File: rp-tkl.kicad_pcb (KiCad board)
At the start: 2 copper layers, 344.7 x 123.1 mm, 0 parts

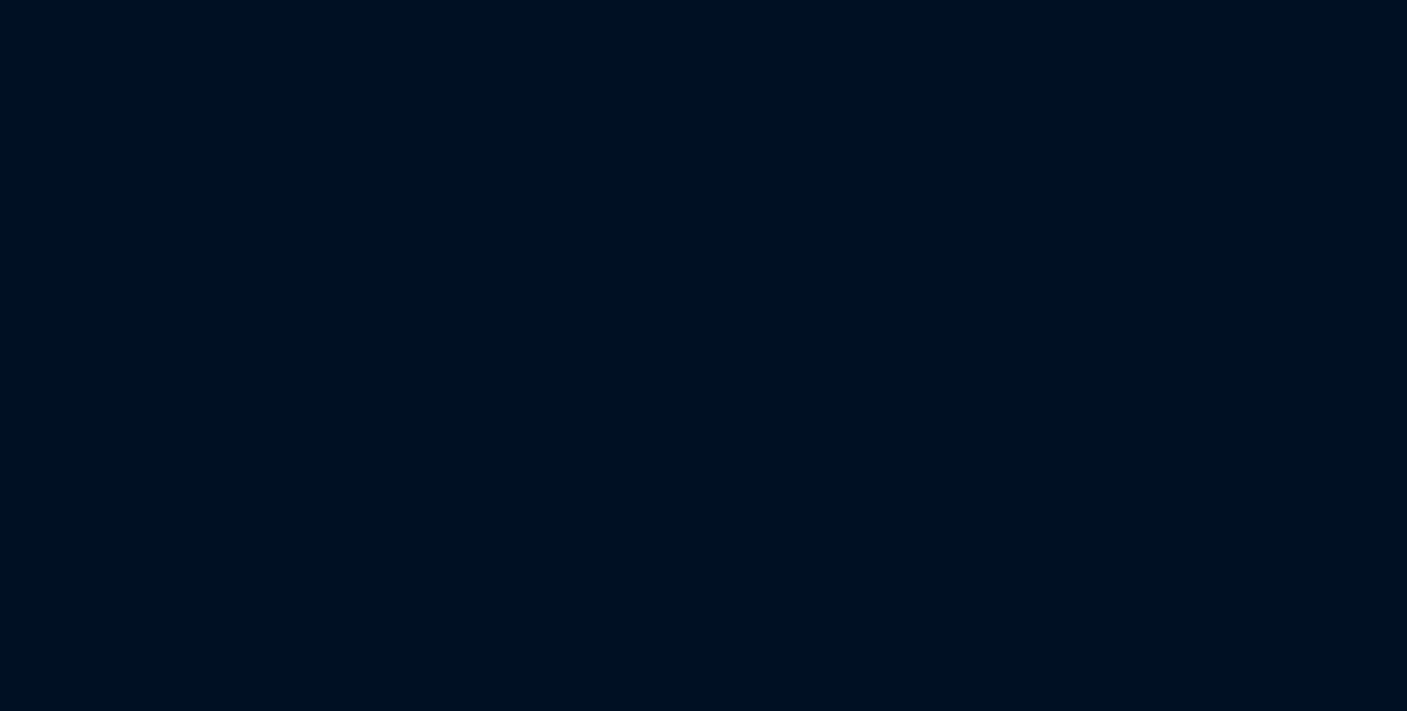
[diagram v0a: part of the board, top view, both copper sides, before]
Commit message: Added Footprint Libs, Annotated schematic, Imported footprints
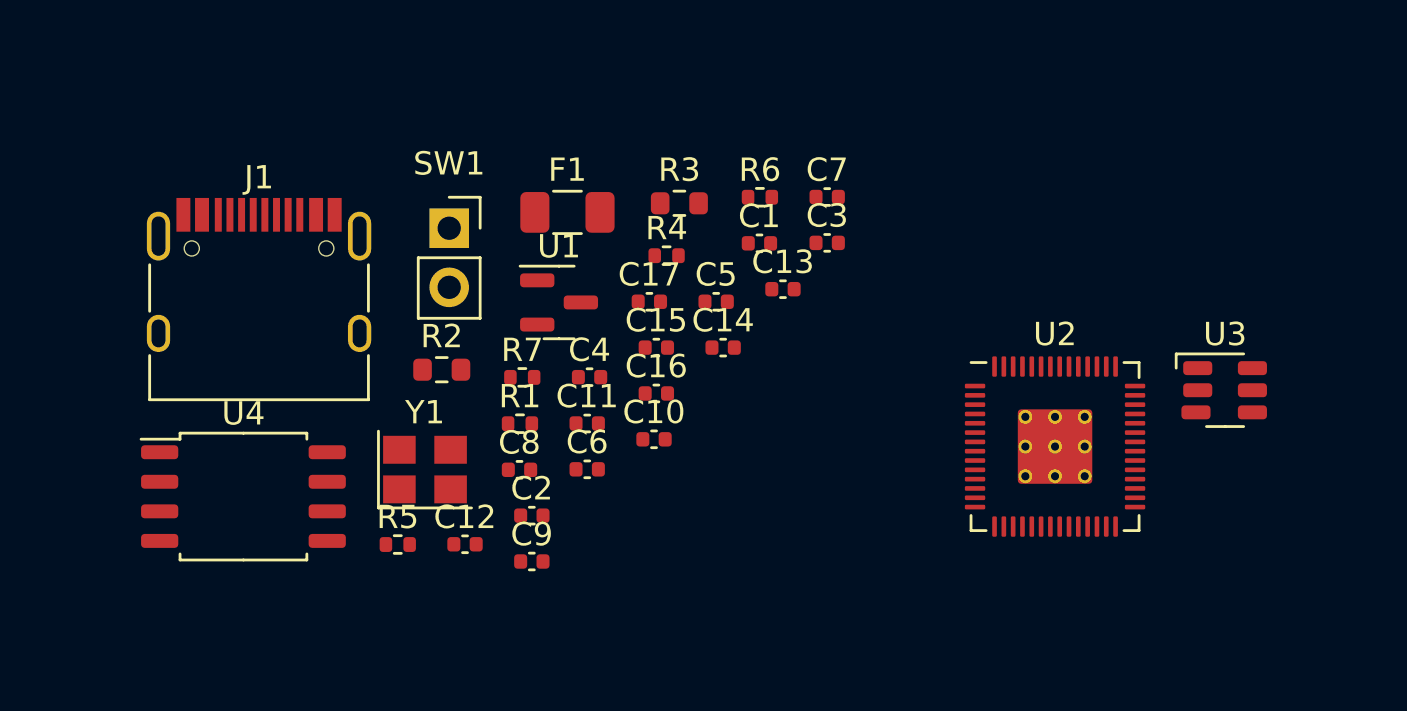
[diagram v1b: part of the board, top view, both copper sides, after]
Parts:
- added C1: 1uF, Capacitor_SMD:C_0402_1005Metric, F.Cu at (213.9, 104.2)
- added C10: 100nF, Capacitor_SMD:C_0402_1005Metric, F.Cu at (209.4, 112.6)
- added C11: 100nF, Capacitor_SMD:C_0402_1005Metric, F.Cu at (206.5, 111.9)
- added C12: 100nF, Capacitor_SMD:C_0402_1005Metric, F.Cu at (201.3, 117.1)
- added C13: 1uF, Capacitor_SMD:C_0402_1005Metric, F.Cu at (214.9, 106.2)
- added C14: 1uF, Capacitor_SMD:C_0402_1005Metric, F.Cu at (212.4, 108.7)
- added C15: 22pF, Capacitor_SMD:C_0402_1005Metric, F.Cu at (209.5, 108.7)
- added C16: 22pF, Capacitor_SMD:C_0402_1005Metric, F.Cu at (209.5, 110.6)
- added C17: 100nF, Capacitor_SMD:C_0402_1005Metric, F.Cu at (209.2, 106.7)
- added C2: 100nF, Capacitor_SMD:C_0402_1005Metric, F.Cu at (204.1, 115.9)
- added C3: 100nF, Capacitor_SMD:C_0402_1005Metric, F.Cu at (216.8, 104.2)
- added C4: 10uF, Capacitor_SMD:C_0402_1005Metric, F.Cu at (206.6, 109.9)
- added C5: 1uF, Capacitor_SMD:C_0402_1005Metric, F.Cu at (212.1, 106.7)
- added C6: 100nF, Capacitor_SMD:C_0402_1005Metric, F.Cu at (206.5, 113.9)
- added C7: 100nF, Capacitor_SMD:C_0402_1005Metric, F.Cu at (216.8, 102.2)
- added C8: 100nF, Capacitor_SMD:C_0402_1005Metric, F.Cu at (203.6, 113.9)
- added C9: 100nF, Capacitor_SMD:C_0402_1005Metric, F.Cu at (204.1, 117.9)
- added F1: 500mA, Fuse:Fuse_1206_3216Metric, F.Cu at (205.7, 102.9)
- added J1: USB_C_Receptacle_USB2.0, Connector_USB:USB_C_Receptacle_HRO_TYPE-C-31-M-12, F.Cu at (192.4, 107.0)
- added R1: 10k, Resistor_SMD:R_0402_1005Metric, F.Cu at (203.6, 111.9)
- added R2: 27R, Resistor_SMD:R_0603_1608Metric, F.Cu at (200.3, 109.6)
- added R3: 27R, Resistor_SMD:R_0603_1608Metric, F.Cu at (210.5, 102.5)
- added R4: 1k, Resistor_SMD:R_0402_1005Metric, F.Cu at (209.9, 104.7)
- added R5: 1k, Resistor_SMD:R_0402_1005Metric, F.Cu at (198.4, 117.1)
- added R6: 5.1k, Resistor_SMD:R_0402_1005Metric, F.Cu at (213.9, 102.2)
- added R7: 5.1k, Resistor_SMD:R_0402_1005Metric, F.Cu at (203.7, 110.0)
- added SW1: SW_Push, Connector_PinSocket_2.54mm:PinSocket_1x02_P2.54mm_Vertical, F.Cu at (200.6, 103.5)
- added U1: XC6206PxxxMR, Package_TO_SOT_SMD:SOT-23, F.Cu at (205.3, 106.7)
- added U2: RP2040, Sleep-lib:RP2040-QFN-56, F.Cu at (226.6, 112.9)
- added U3: SRV05-4, marbastlib-various:SOT-23-6-routable, F.Cu at (233.9, 110.5)
- added U4: W25Q128JVS, Package_SO:SOIC-8_5.23x5.23mm_P1.27mm, F.Cu at (191.8, 115.1)
- added Y1: 12MHz, Crystal:Crystal_SMD_3225-4Pin_3.2x2.5mm, F.Cu at (199.6, 113.9)

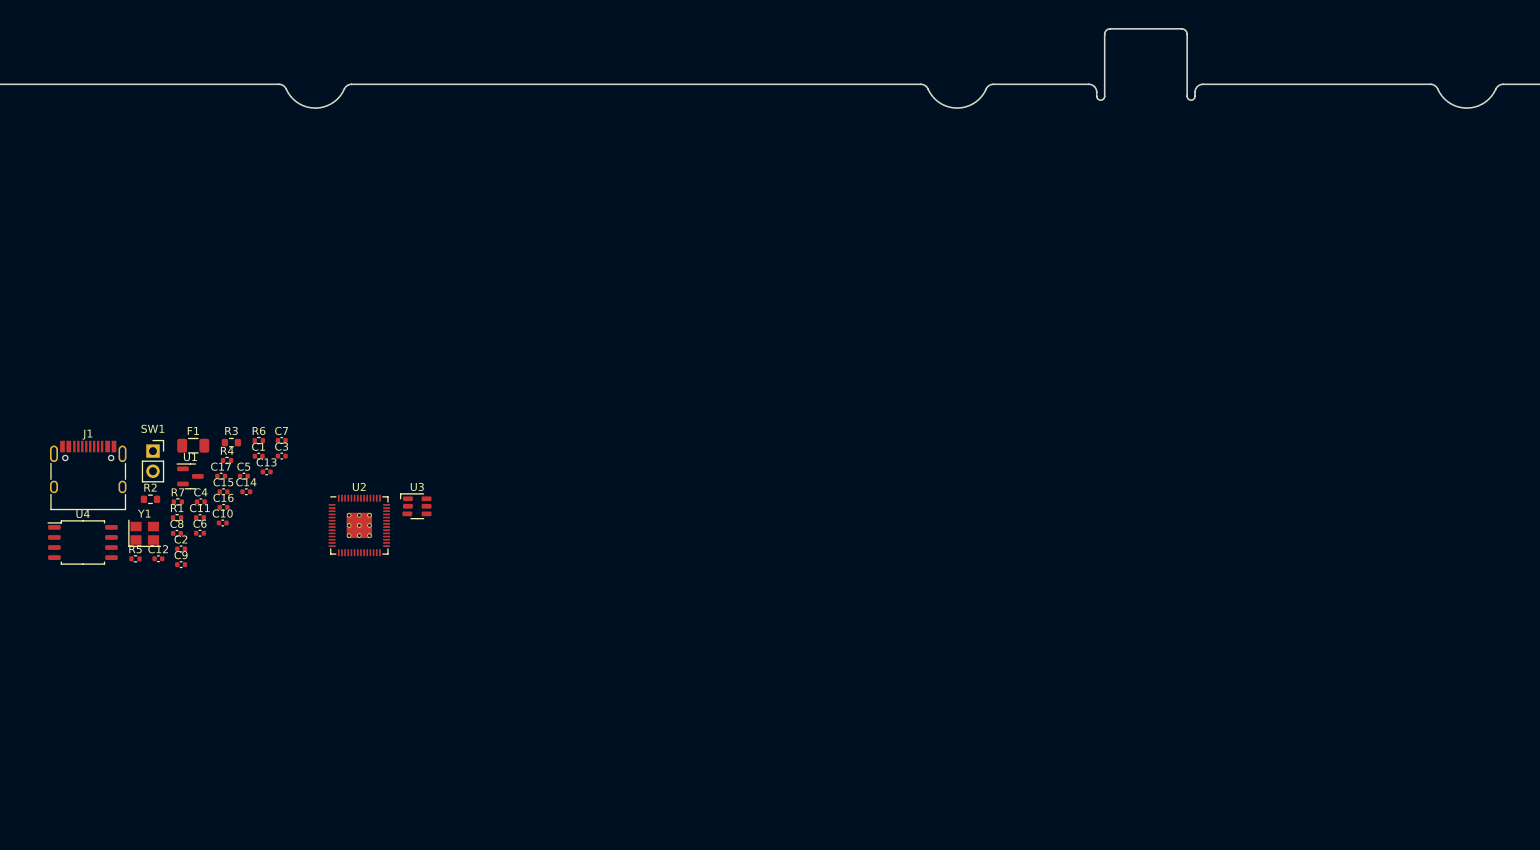
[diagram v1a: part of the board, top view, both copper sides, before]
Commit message: [Excluding Switches] Moved components to rough positions on pcb
Also added 5 pin programming header
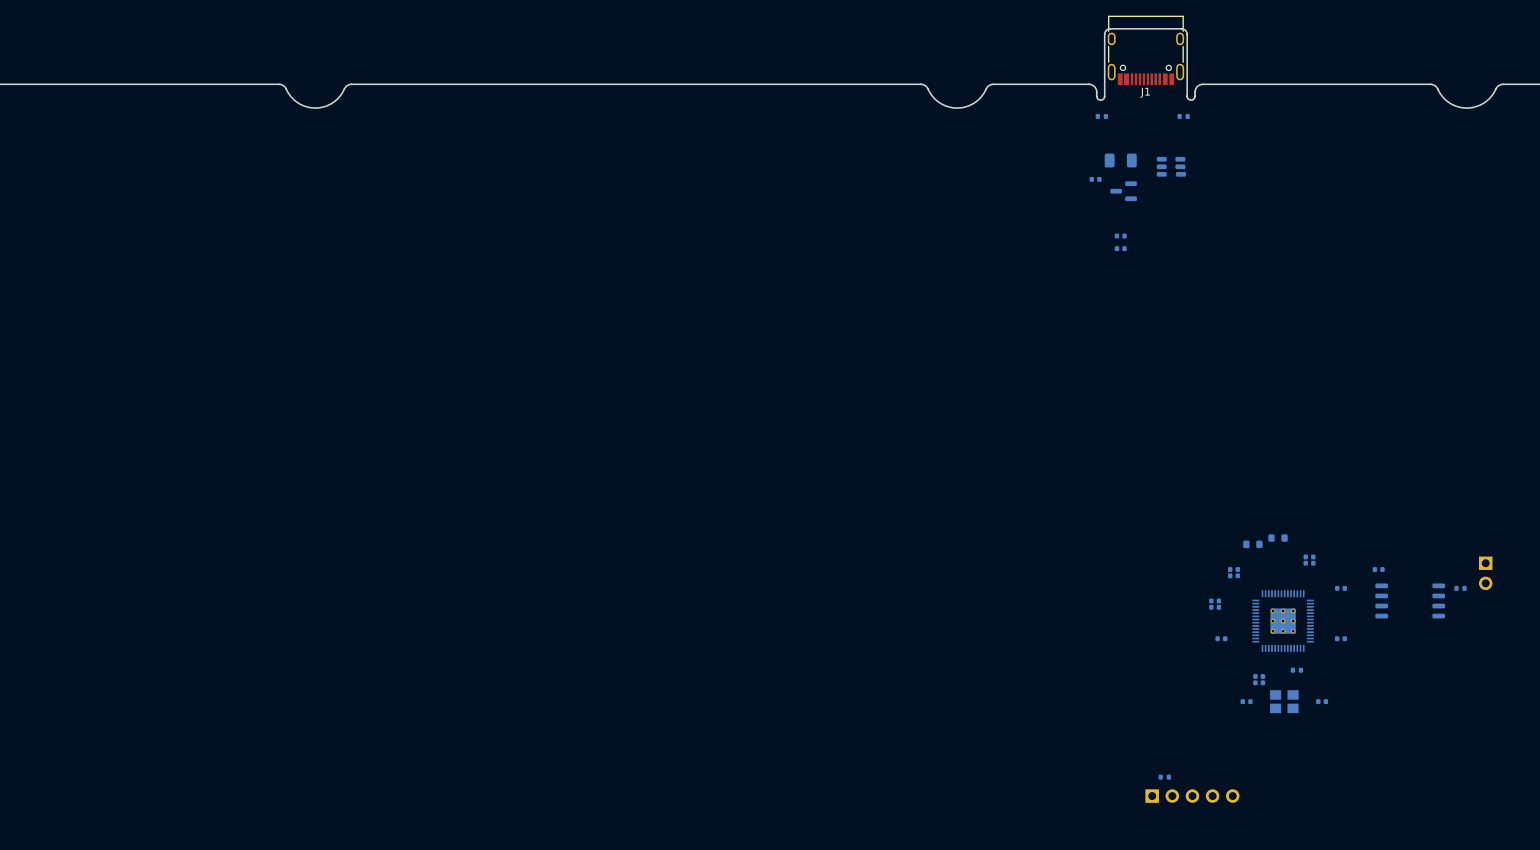
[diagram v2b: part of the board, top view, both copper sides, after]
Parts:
- added J2: SWD, Connector_PinSocket_2.54mm:PinSocket_1x05_P2.54mm_Vertical, B.Cu at (326.6, 147.1)
- C1, C10, C11, C12, C13, C14, C15, C16, C17, C2, C3, C4, C5, C6, C7, C8, C9, F1, R1, R2, R3, R4, R5, R6, R7, SW1, U1, U2, U3, U4, Y1: moved to B.Cu
- moved SW1 168.7 mm to (368.7, 117.7), turned to 180 degrees
- moved U4 167.6 mm to (359.2, 122.5), turned to 180 degrees
- moved R5 167.2 mm to (365.5, 120.9), turned to 180 degrees
- moved C12 149.2 mm to (350.5, 120.9), turned to 180 degrees
- moved C8 147.4 mm to (350.5, 127.2), turned to 180 degrees
- moved C17 146.5 mm to (355.2, 118.5), turned to 180 degrees
- moved Y1 145.3 mm to (343.3, 135.2), turned to 180 degrees
- moved J1 144.1 mm to (325.8, 52.6), turned to 180 degrees
- moved C16 140.7 mm to (348.1, 135.2), turned to 180 degrees
- moved R2 139.2 mm to (339.3, 115.3), turned to 180 degrees
- moved R4 137.5 mm to (344.9, 131.2), turned to 180 degrees
- moved C2 136.9 mm to (340.1, 132.0), turned to 180 degrees
- moved C9 136.8 mm to (340.1, 132.8), turned to 180 degrees
- moved R3 132.6 mm to (342.5, 114.5), turned to 180 degrees
- moved C15 131.7 mm to (338.5, 135.2), turned to 180 degrees
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
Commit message: [Preliminary] Added Switch matrix and imported footprints
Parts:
- added D1: D, Diode_SMD:D_0402_1005Metric, B.Cu at (686.1, 243.1)
- added D10: D, Diode_SMD:D_0402_1005Metric, B.Cu at (466.5, 79.8)
- added D11: D, Diode_SMD:D_0402_1005Metric, B.Cu at (723.8, 241.1)
- added D12: D, Diode_SMD:D_0402_1005Metric, B.Cu at (705.0, 241.1)
- added D13: D, Diode_SMD:D_0402_1005Metric, B.Cu at (506.9, 120.1)
- added D14: D, Diode_SMD:D_0402_1005Metric, B.Cu at (726.9, 241.1)
- added D15: D, Diode_SMD:D_0402_1005Metric, B.Cu at (446.4, 59.6)
- added D16: D, Diode_SMD:D_0402_1005Metric, B.Cu at (698.7, 241.1)
- added D17: D, Diode_SMD:D_0402_1005Metric, B.Cu at (629.6, 243.1)
- added D18: D, Diode_SMD:D_0402_1005Metric, B.Cu at (739.5, 241.1)
- added D19: D, Diode_SMD:D_0402_1005Metric, B.Cu at (645.3, 241.1)
- added D2: D, Diode_SMD:D_0402_1005Metric, B.Cu at (673.6, 241.1)
- added D20: D, Diode_SMD:D_0402_1005Metric, B.Cu at (446.4, 61.6)
- added D21: D, Diode_SMD:D_0402_1005Metric, B.Cu at (506.9, 122.1)
- added D22: D, Diode_SMD:D_0402_1005Metric, B.Cu at (486.7, 101.9)
- added D23: D, Diode_SMD:D_0402_1005Metric, B.Cu at (654.7, 241.1)
- added D24: D, Diode_SMD:D_0402_1005Metric, B.Cu at (745.8, 241.1)
- added D25: D, Diode_SMD:D_0402_1005Metric, B.Cu at (483.6, 99.9)
- added D26: D, Diode_SMD:D_0402_1005Metric, B.Cu at (679.8, 241.1)
- added D27: D, Diode_SMD:D_0402_1005Metric, B.Cu at (717.5, 241.1)
- added D28: D, Diode_SMD:D_0402_1005Metric, B.Cu at (733.2, 243.1)
- added D29: D, Diode_SMD:D_0402_1005Metric, B.Cu at (664.1, 241.1)
- added D3: D, Diode_SMD:D_0402_1005Metric, B.Cu at (711.2, 243.1)
- added D30: D, Diode_SMD:D_0402_1005Metric, B.Cu at (651.6, 241.1)
- added D31: D, Diode_SMD:D_0402_1005Metric, B.Cu at (692.4, 241.1)
- added D32: D, Diode_SMD:D_0402_1005Metric, B.Cu at (676.7, 243.1)
- added D33: D, Diode_SMD:D_0402_1005Metric, B.Cu at (670.4, 241.1)
- added D34: D, Diode_SMD:D_0402_1005Metric, B.Cu at (708.1, 241.1)
- added D35: D, Diode_SMD:D_0402_1005Metric, B.Cu at (654.7, 243.1)
- added D36: D, Diode_SMD:D_0402_1005Metric, B.Cu at (632.7, 243.1)
- added D37: D, Diode_SMD:D_0402_1005Metric, B.Cu at (720.7, 243.1)
- added D38: D, Diode_SMD:D_0402_1005Metric, B.Cu at (683.0, 243.1)
- added D39: D, Diode_SMD:D_0402_1005Metric, B.Cu at (639.0, 241.1)
- added D4: D, Diode_SMD:D_0402_1005Metric, B.Cu at (657.9, 243.1)
- added D40: D, Diode_SMD:D_0402_1005Metric, B.Cu at (629.6, 241.1)
- added D41: D, Diode_SMD:D_0402_1005Metric, B.Cu at (664.1, 243.1)
- added D42: D, Diode_SMD:D_0402_1005Metric, B.Cu at (692.4, 243.1)
- added D43: D, Diode_SMD:D_0402_1005Metric, B.Cu at (651.6, 243.1)
- added D44: D, Diode_SMD:D_0402_1005Metric, B.Cu at (648.4, 241.1)
- added D45: D, Diode_SMD:D_0402_1005Metric, B.Cu at (730.1, 243.1)
- added D46: D, Diode_SMD:D_0402_1005Metric, B.Cu at (748.9, 241.1)
- added D47: D, Diode_SMD:D_0402_1005Metric, B.Cu at (701.8, 241.1)
- added D48: D, Diode_SMD:D_0402_1005Metric, B.Cu at (642.2, 241.1)
- added D49: D, Diode_SMD:D_0402_1005Metric, B.Cu at (679.8, 243.1)
- added D5: D, Diode_SMD:D_0402_1005Metric, B.Cu at (714.4, 243.1)
- added D50: D, Diode_SMD:D_0402_1005Metric, B.Cu at (720.7, 241.1)
- added D51: D, Diode_SMD:D_0402_1005Metric, B.Cu at (639.0, 243.1)
- added D52: D, Diode_SMD:D_0402_1005Metric, B.Cu at (657.9, 241.1)
- added D53: D, Diode_SMD:D_0402_1005Metric, B.Cu at (683.0, 241.1)
- added D54: D, Diode_SMD:D_0402_1005Metric, B.Cu at (689.3, 243.1)
- added D55: D, Diode_SMD:D_0402_1005Metric, B.Cu at (661.0, 241.1)
- added D56: D, Diode_SMD:D_0402_1005Metric, B.Cu at (635.9, 241.1)
- added D57: D, Diode_SMD:D_0402_1005Metric, B.Cu at (466.5, 81.7)
- added D58: D, Diode_SMD:D_0402_1005Metric, B.Cu at (689.3, 241.1)
- added D59: D, Diode_SMD:D_0402_1005Metric, B.Cu at (635.9, 243.1)
- added D6: D, Diode_SMD:D_0402_1005Metric, B.Cu at (742.6, 241.1)
- added D60: D, Diode_SMD:D_0402_1005Metric, B.Cu at (717.5, 243.1)
- added D61: D, Diode_SMD:D_0402_1005Metric, B.Cu at (443.2, 59.6)
- added D62: D, Diode_SMD:D_0402_1005Metric, B.Cu at (686.1, 241.1)
- added D63: D, Diode_SMD:D_0402_1005Metric, B.Cu at (648.4, 243.1)
- added D64: D, Diode_SMD:D_0402_1005Metric, B.Cu at (626.5, 241.1)
- added D65: D, Diode_SMD:D_0402_1005Metric, B.Cu at (463.4, 79.8)
- added D66: D, Diode_SMD:D_0402_1005Metric, B.Cu at (486.7, 99.9)
- added D67: D, Diode_SMD:D_0402_1005Metric, B.Cu at (730.1, 241.1)
- added D68: D, Diode_SMD:D_0402_1005Metric, B.Cu at (695.5, 243.1)
- added D69: D, Diode_SMD:D_0402_1005Metric, B.Cu at (705.0, 243.1)
- added D7: D, Diode_SMD:D_0402_1005Metric, B.Cu at (742.6, 243.1)
- added D70: D, Diode_SMD:D_0402_1005Metric, B.Cu at (503.7, 120.1)
- added D71: D, Diode_SMD:D_0402_1005Metric, B.Cu at (736.4, 243.1)
- added D72: D, Diode_SMD:D_0402_1005Metric, B.Cu at (676.7, 241.1)
- added D73: D, Diode_SMD:D_0402_1005Metric, B.Cu at (632.7, 241.1)
- added D74: D, Diode_SMD:D_0402_1005Metric, B.Cu at (739.5, 243.1)
- added D75: D, Diode_SMD:D_0402_1005Metric, B.Cu at (711.2, 241.1)
- added D76: D, Diode_SMD:D_0402_1005Metric, B.Cu at (670.4, 243.1)
- added D77: D, Diode_SMD:D_0402_1005Metric, B.Cu at (723.8, 243.1)
- added D78: D, Diode_SMD:D_0402_1005Metric, B.Cu at (667.3, 241.1)
- added D79: D, Diode_SMD:D_0402_1005Metric, B.Cu at (714.4, 241.1)
- added D8: D, Diode_SMD:D_0402_1005Metric, B.Cu at (726.9, 243.1)
- added D80: D, Diode_SMD:D_0402_1005Metric, B.Cu at (745.8, 243.1)
- added D81: D, Diode_SMD:D_0402_1005Metric, B.Cu at (642.2, 243.1)
- added D82: D, Diode_SMD:D_0402_1005Metric, B.Cu at (645.3, 243.1)
- added D83: D, Diode_SMD:D_0402_1005Metric, B.Cu at (733.2, 241.1)
- added D84: D, Diode_SMD:D_0402_1005Metric, B.Cu at (698.7, 243.1)
- added D85: D, Diode_SMD:D_0402_1005Metric, B.Cu at (695.5, 241.1)
- added D86: D, Diode_SMD:D_0402_1005Metric, B.Cu at (673.6, 243.1)
- added D87: D, Diode_SMD:D_0402_1005Metric, B.Cu at (667.3, 243.1)
- added D88: D, Diode_SMD:D_0402_1005Metric, B.Cu at (701.8, 243.1)
- added D89: D, Diode_SMD:D_0402_1005Metric, B.Cu at (748.9, 243.1)
- added D9: D, Diode_SMD:D_0402_1005Metric, B.Cu at (708.1, 243.1)
- added D90: D, Diode_SMD:D_0402_1005Metric, B.Cu at (736.4, 241.1)
- added D91: D, Diode_SMD:D_0402_1005Metric, B.Cu at (661.0, 243.1)
- added SW10: ?, marbastlib-mx:SW_MX_HS_1u, B.Cu at (700.2, 230.0)
- added SW100: ?, marbastlib-mx:SW_MX_HS_1u, B.Cu at (498.5, 109.0)
- added SW101: ?, marbastlib-mx:SW_MX_HS_1u, B.Cu at (740.5, 230.0)
- added SW102: ?, marbastlib-mx:SW_MX_HS_1u, B.Cu at (478.3, 88.8)
- added SW103: ?, marbastlib-mx:SW_MX_HS_1u, B.Cu at (700.2, 109.0)
- added SW104: ?, marbastlib-mx:SW_MX_HS_1u, B.Cu at (619.5, 68.7)
- added SW105: ?, marbastlib-mx:SW_MX_HS_1u, B.Cu at (740.5, 68.7)
- added SW11: ?, marbastlib-mx:SW_MX_HS_1u, B.Cu at (720.4, 109.0)
- added SW12: ?, marbastlib-mx:SW_MX_HS_1u, B.Cu at (538.8, 129.2)
- added SW13: ?, marbastlib-mx:SW_MX_HS_1u, B.Cu at (720.4, 169.5)
- added SW14: ?, marbastlib-mx:SW_MX_HS_1u, B.Cu at (680.0, 149.4)
- added SW15: ?, marbastlib-mx:SW_MX_HS_1u, B.Cu at (559.0, 88.8)
- added SW16: ?, marbastlib-mx:SW_MX_HS_1u, B.Cu at (740.5, 189.7)
- added SW17: ?, marbastlib-mx:SW_MX_HS_1u, B.Cu at (740.5, 149.4)
- added SW18: ?, marbastlib-mx:SW_MX_HS_1u, B.Cu at (599.3, 129.2)
- added SW19: ?, marbastlib-mx:SW_MX_HS_1u, B.Cu at (538.8, 68.7)
- added SW2: ?, marbastlib-mx:SW_MX_HS_1u, B.Cu at (579.2, 209.9)
- added SW20: ?, marbastlib-mx:SW_MX_HS_1u, B.Cu at (579.2, 109.0)
- added SW21: ?, marbastlib-mx:SW_MX_HS_1u, B.Cu at (659.8, 209.9)
- added SW22: ?, marbastlib-mx:SW_MX_HS_1u, B.Cu at (720.4, 129.2)
- added SW23: ?, marbastlib-mx:SW_MX_HS_1u, B.Cu at (559.0, 189.7)
- added SW24: ?, marbastlib-mx:SW_MX_HS_1u, B.Cu at (639.7, 129.2)
- added SW25: ?, marbastlib-mx:SW_MX_HS_1u, B.Cu at (680.0, 88.8)
- added SW26: ?, marbastlib-mx:SW_MX_HS_1u, B.Cu at (599.3, 230.0)
- added SW27: ?, marbastlib-mx:SW_MX_HS_1u, B.Cu at (680.0, 230.0)
- added SW28: ?, marbastlib-mx:SW_MX_HS_1u, B.Cu at (518.7, 149.4)
- added SW29: ?, marbastlib-mx:SW_MX_HS_1u, B.Cu at (599.3, 68.7)
- added SW3: ?, marbastlib-mx:SW_MX_HS_1u, B.Cu at (659.8, 189.7)
- added SW30: ?, marbastlib-mx:SW_MX_HS_1u, B.Cu at (579.2, 149.4)
- added SW31: ?, marbastlib-mx:SW_MX_HS_1u, B.Cu at (538.8, 88.8)
- added SW32: ?, marbastlib-mx:SW_MX_HS_1u, B.Cu at (720.4, 149.4)
- added SW33: ?, marbastlib-mx:SW_MX_HS_1u, B.Cu at (619.5, 230.0)
- added SW34: ?, marbastlib-mx:SW_MX_HS_1u, B.Cu at (619.5, 189.7)
- added SW35: ?, marbastlib-mx:SW_MX_HS_1u, B.Cu at (680.0, 189.7)
- added SW36: ?, marbastlib-mx:SW_MX_HS_1u, B.Cu at (559.0, 169.5)
- added SW37: ?, marbastlib-mx:SW_MX_HS_1u, B.Cu at (700.2, 149.4)
- added SW38: ?, marbastlib-mx:SW_MX_HS_1u, B.Cu at (579.2, 169.5)
- added SW39: ?, marbastlib-mx:SW_MX_HS_1u, B.Cu at (518.7, 129.2)
- added SW4: ?, marbastlib-mx:SW_MX_HS_1u, B.Cu at (559.0, 149.4)
- added SW40: ?, marbastlib-mx:SW_MX_HS_1u, B.Cu at (659.8, 88.8)
- added SW41: ?, marbastlib-mx:SW_MX_HS_1u, B.Cu at (498.5, 68.7)
- added SW42: ?, marbastlib-mx:SW_MX_HS_1u, B.Cu at (639.7, 209.9)
- added SW43: ?, marbastlib-mx:SW_MX_HS_1u, B.Cu at (700.2, 68.7)
- added SW44: ?, marbastlib-mx:SW_MX_HS_1u, B.Cu at (518.7, 109.0)
- added SW45: ?, marbastlib-mx:SW_MX_HS_1u, B.Cu at (559.0, 68.7)
- added SW46: ?, marbastlib-mx:SW_MX_HS_1u, B.Cu at (559.0, 129.2)
- added SW47: ?, marbastlib-mx:SW_MX_HS_1u, B.Cu at (579.2, 68.7)
- added SW48: ?, marbastlib-mx:SW_MX_HS_1u, B.Cu at (659.8, 230.0)
- added SW49: ?, marbastlib-mx:SW_MX_HS_1u, B.Cu at (619.5, 129.2)
- added SW5: ?, marbastlib-mx:SW_MX_HS_1u, B.Cu at (639.7, 149.4)
- added SW50: ?, marbastlib-mx:SW_MX_HS_1u, B.Cu at (680.0, 209.9)
- added SW51: ?, marbastlib-mx:SW_MX_HS_1u, B.Cu at (700.2, 169.5)
- added SW52: ?, marbastlib-mx:SW_MX_HS_1u, B.Cu at (740.5, 209.9)
- added SW53: ?, marbastlib-mx:SW_MX_HS_1u, B.Cu at (659.8, 149.4)
- added SW54: ?, marbastlib-mx:SW_MX_HS_1u, B.Cu at (639.7, 189.7)
- added SW55: ?, marbastlib-mx:SW_MX_HS_1u, B.Cu at (639.7, 109.0)
- added SW56: ?, marbastlib-mx:SW_MX_HS_1u, B.Cu at (599.3, 209.9)
- added SW57: ?, marbastlib-mx:SW_MX_HS_1u, B.Cu at (619.5, 209.9)
- added SW58: ?, marbastlib-mx:SW_MX_HS_1u, B.Cu at (659.8, 68.7)
- added SW59: ?, marbastlib-mx:SW_MX_HS_1u, B.Cu at (599.3, 169.5)
- added SW6: ?, marbastlib-mx:SW_MX_HS_1u, B.Cu at (498.5, 88.8)
- added SW60: ?, marbastlib-mx:SW_MX_HS_1u, B.Cu at (740.5, 129.2)
- added SW61: ?, marbastlib-mx:SW_MX_HS_1u, B.Cu at (619.5, 169.5)
- added SW62: ?, marbastlib-mx:SW_MX_HS_1u, B.Cu at (680.0, 169.5)
- added SW63: ?, marbastlib-mx:SW_MX_HS_1u, B.Cu at (680.0, 109.0)
- added SW64: ?, marbastlib-mx:SW_MX_HS_1u, B.Cu at (518.7, 68.7)
- added SW65: ?, marbastlib-mx:SW_MX_HS_1u, B.Cu at (619.5, 149.4)
- added SW66: ?, marbastlib-mx:SW_MX_HS_1u, B.Cu at (700.2, 129.2)
- added SW67: ?, marbastlib-mx:SW_MX_HS_1u, B.Cu at (639.7, 230.0)
- added SW68: ?, marbastlib-mx:SW_MX_HS_1u, B.Cu at (720.4, 68.7)
- added SW69: ?, marbastlib-mx:SW_MX_HS_1u, B.Cu at (579.2, 189.7)
- added SW7: ?, marbastlib-mx:SW_MX_HS_1u, B.Cu at (720.4, 230.0)
- added SW70: ?, marbastlib-mx:SW_MX_HS_1u, B.Cu at (659.8, 169.5)
- added SW71: ?, marbastlib-mx:SW_MX_HS_1u, B.Cu at (478.3, 68.7)
- added SW72: ?, marbastlib-mx:SW_MX_HS_1u, B.Cu at (740.5, 109.0)
- added SW73: ?, marbastlib-mx:SW_MX_HS_1u, B.Cu at (700.2, 88.8)
- added SW74: ?, marbastlib-mx:SW_MX_HS_1u, B.Cu at (538.8, 169.5)
- added SW75: ?, marbastlib-mx:SW_MX_HS_1u, B.Cu at (599.3, 149.4)
- added SW76: ?, marbastlib-mx:SW_MX_HS_1u, B.Cu at (659.8, 109.0)
- added SW77: ?, marbastlib-mx:SW_MX_HS_1u, B.Cu at (720.4, 189.7)
- added SW78: ?, marbastlib-mx:SW_MX_HS_1u, B.Cu at (639.7, 88.8)
- added SW79: ?, marbastlib-mx:SW_MX_HS_1u, B.Cu at (659.8, 129.2)
- added SW8: ?, marbastlib-mx:SW_MX_HS_1u, B.Cu at (680.0, 129.2)
- added SW80: ?, marbastlib-mx:SW_MX_HS_1u, B.Cu at (619.5, 88.8)
- added SW81: ?, marbastlib-mx:SW_MX_HS_1u, B.Cu at (619.5, 109.0)
- added SW82: ?, marbastlib-mx:SW_MX_HS_1u, B.Cu at (579.2, 88.8)
- added SW83: ?, marbastlib-mx:SW_MX_HS_1u, B.Cu at (720.4, 88.8)
- added SW84: ?, marbastlib-mx:SW_MX_HS_1u, B.Cu at (680.0, 68.7)
- added SW85: ?, marbastlib-mx:SW_MX_HS_1u, B.Cu at (458.1, 68.7)
- added SW86: ?, marbastlib-mx:SW_MX_HS_1u, B.Cu at (639.7, 68.7)
- added SW87: ?, marbastlib-mx:SW_MX_HS_1u, B.Cu at (720.4, 209.9)
- added SW88: ?, marbastlib-mx:SW_MX_HS_1u, B.Cu at (599.3, 189.7)
- added SW89: ?, marbastlib-mx:SW_MX_HS_1u, B.Cu at (559.0, 109.0)
- added SW9: ?, marbastlib-mx:SW_MX_HS_1u, B.Cu at (599.3, 88.8)
- added SW90: ?, marbastlib-mx:SW_MX_HS_1u, B.Cu at (538.8, 149.4)
- added SW91: ?, marbastlib-mx:SW_MX_HS_1u, B.Cu at (740.5, 88.8)
- added SW92: ?, marbastlib-mx:SW_MX_HS_1u, B.Cu at (700.2, 209.9)
- added SW93: ?, marbastlib-mx:SW_MX_HS_1u, B.Cu at (538.8, 109.0)
- added SW94: ?, marbastlib-mx:SW_MX_HS_1u, B.Cu at (518.7, 88.8)
- added SW95: ?, marbastlib-mx:SW_MX_HS_1u, B.Cu at (740.5, 169.5)
- added SW96: ?, marbastlib-mx:SW_MX_HS_1u, B.Cu at (599.3, 109.0)
- added SW97: ?, marbastlib-mx:SW_MX_HS_1u, B.Cu at (700.2, 189.7)
- added SW98: ?, marbastlib-mx:SW_MX_HS_1u, B.Cu at (639.7, 169.5)
- added SW99: ?, marbastlib-mx:SW_MX_HS_1u, B.Cu at (579.2, 129.2)
